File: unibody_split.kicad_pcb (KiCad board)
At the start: 2 copper layers, 305.5 x 82.5 mm, 92 parts, among them J1 Conn_01x02, U1 nice_nano

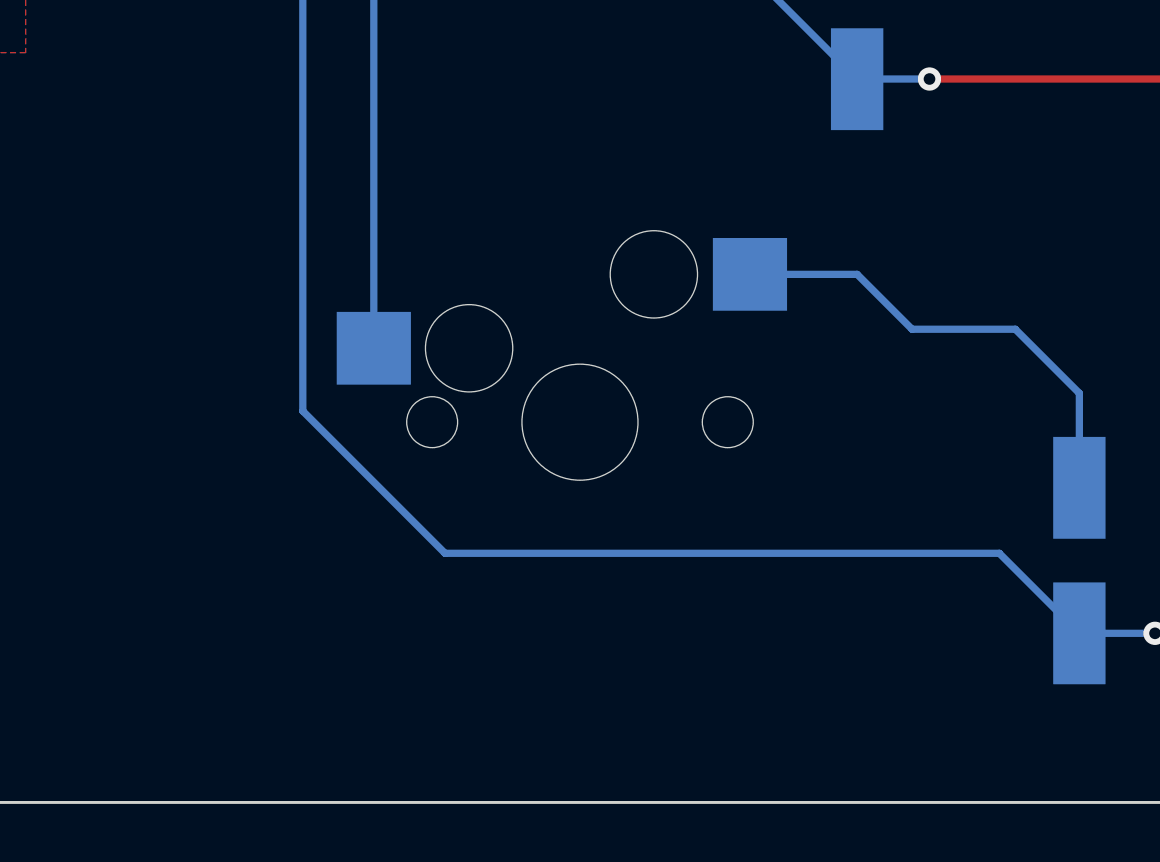
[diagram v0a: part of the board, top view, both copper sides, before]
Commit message: Fixes M29 using wrong footprint
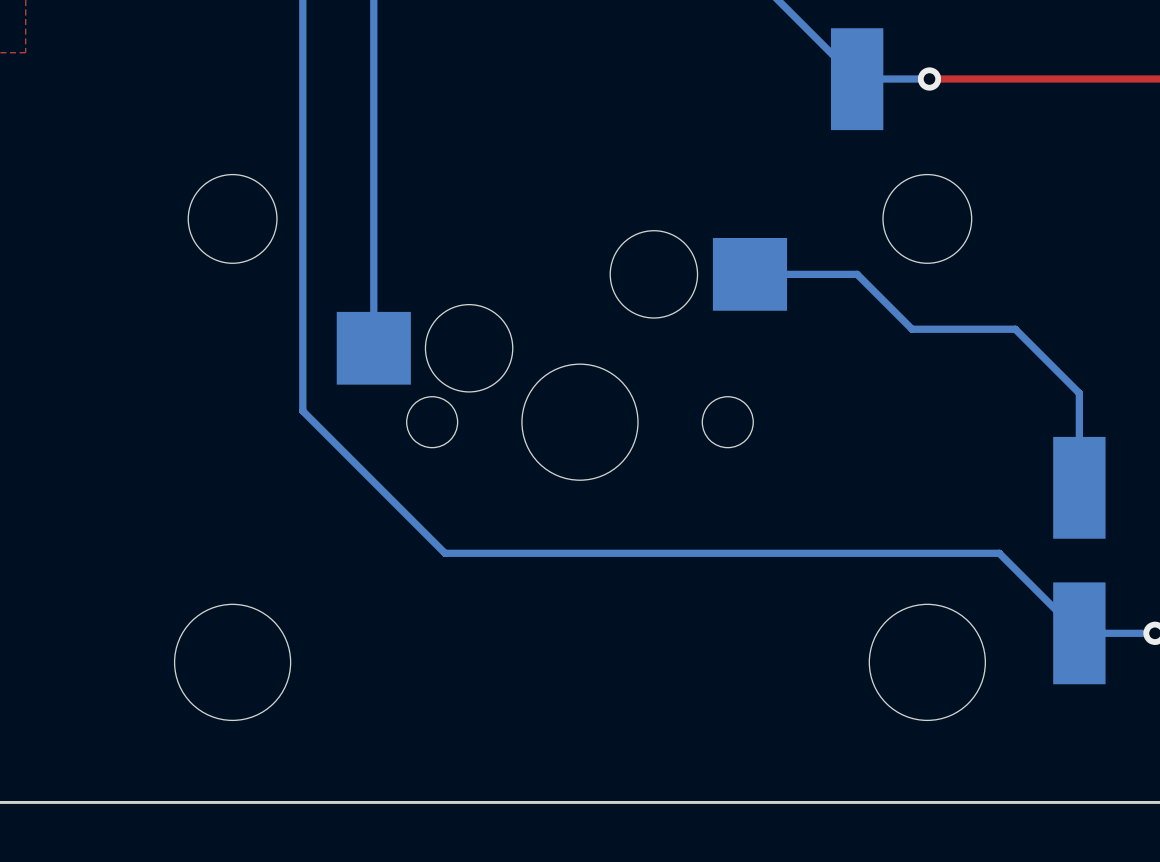
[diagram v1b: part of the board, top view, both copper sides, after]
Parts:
- MX29: footprint MX_Only:MXOnly-1U-Hotswap -> MX_Only:MXOnly-2U-Hotswap
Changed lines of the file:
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@@
     )
   )
-  (footprint "MX_Only:MXOnly-1U-Hotswap" (layer "F.Cu")
+  (footprint "MX_Only:MXOnly-2U-Hotswap" (layer "F.Cu")
     (at 255.5875 165.89375)
     (property "Sheetfile" "unibody_split.kicad_sch")
@@
       (effects (font (size 1 1) (thickness 0.15)))
     )
+    (fp_line (start 19.05 -9.525) (end 19.05 9.525) (layer "Dwgs.User") (width 0.15))
+    (fp_line (start -7 7) (end -5 7) (layer "Dwgs.User") (width 0.15))
+    (fp_line (start 19.05 9.525) (end -19.05 9.525) (layer "Dwgs.User") (width 0.15))
     (fp_line (start -7 -7) (end -7 -5) (layer "Dwgs.User") (width 0.15))
-    (fp_line (start -7 7) (end -5 7) (layer "Dwgs.User") (width 0.15))
+    (fp_line (start 5 -7) (end 7 -7) (layer "Dwgs.User") (width 0.15))
+    (fp_line (start 5 7) (end 7 7) (layer "Dwgs.User") (width 0.15))
+    (fp_line (start 7 7) (end 7 5) (layer "Dwgs.User") (width 0.15))
+    (fp_line (start -7 5) (end -7 7) (layer "Dwgs.User") (width 0.15))
+    (fp_line (start -19.05 9.525) (end -19.05 -9.525) (layer "Dwgs.User") (width 0.15))
+    (fp_line (start -5 -7) (end -7 -7) (layer "Dwgs.User") (width 0.15))
     (fp_line (start 7 -7) (end 7 -5) (layer "Dwgs.User") (width 0.15))
-    (fp_line (start -5 -7) (end -7 -7) (layer "Dwgs.User") (width 0.15))
-    (fp_line (start 7 7) (end 7 5) (layer "Dwgs.User") (width 0.15))
-    (fp_line (start -9.525 -9.525) (end 9.525 -9.525) (layer "Dwgs.User") (width 0.15))
-    (fp_line (start 9.525 -9.525) (end 9.525 9.525) (layer "Dwgs.User") (width 0.15))
-    (fp_line (start -9.525 9.525) (end -9.525 -9.525) (layer "Dwgs.User") (width 0.15))
-    (fp_line (start -7 5) (end -7 7) (layer "Dwgs.User") (width 0.15))
-    (fp_line (start 9.525 9.525) (end -9.525 9.525) (layer "Dwgs.User") (width 0.15))
-    (fp_line (start 5 7) (end 7 7) (layer "Dwgs.User") (width 0.15))
-    (fp_line (start 5 -7) (end 7 -7) (layer "Dwgs.User") (width 0.15))
+    (fp_line (start -19.05 -9.525) (end 19.05 -9.525) (layer "Dwgs.User") (width 0.15))
+    (fp_line (start 7.112 -3.81) (end 4.572 -3.81) (layer "B.CrtYd") (width 0.15))
+    (fp_line (start 5.3 -7) (end 5.3 -2.6) (layer "B.CrtYd") (width 0.127))
+    (fp_line (start -8.382 -3.81) (end -5.842 -3.81) (layer "B.CrtYd") (width 0.15))
+    (fp_line (start -6.5 -4.5) (end -6.5 -0.6) (layer "B.CrtYd") (width 0.127))
+    (fp_line (start -8.382 -1.27) (end -8.382 -3.81) (layer "B.CrtYd") (width 0.15))
     (fp_line (start -6.5 -0.6) (end -2.4 -0.6) (layer "B.CrtYd") (width 0.127))
-    (fp_line (start -5.842 -1.27) (end -5.842 -3.81) (layer "B.CrtYd") (width 0.15))
-    (fp_line (start 5.3 -7) (end 5.3 -2.6) (layer "B.CrtYd") (width 0.127))
-    (fp_line (start 7.112 -3.81) (end 4.572 -3.81) (layer "B.CrtYd") (width 0.15))
-    (fp_line (start -8.382 -3.81) (end -8.382 -1.27) (layer "B.CrtYd") (width 0.15))
+    (fp_line (start -5.842 -3.81) (end -5.842 -1.27) (layer "B.CrtYd") (width 0.15))
+    (fp_line (start 4.572 -6.35) (end 7.112 -6.35) (layer "B.CrtYd") (width 0.15))
+    (fp_line (start -5.842 -1.27) (end -8.382 -1.27) (layer "B.CrtYd") (width 0.15))
+    (fp_line (start 5.3 -7) (end -4 -7) (layer "B.CrtYd") (width 0.127))
     (fp_line (start 4.572 -3.81) (end 4.572 -6.35) (layer "B.CrtYd") (width 0.15))
-    (fp_line (start -8.382 -1.27) (end -5.842 -1.27) (layer "B.CrtYd") (width 0.15))
-    (fp_line (start -6.5 -4.5) (end -6.5 -0.6) (layer "B.CrtYd") (width 0.127))
-    (fp_line (start 4.572 -6.35) (end 7.112 -6.35) (layer "B.CrtYd") (width 0.15))
-    (fp_line (start -5.842 -3.81) (end -8.382 -3.81) (layer "B.CrtYd") (width 0.15))
+    (fp_line (start 7.112 -6.35) (end 7.112 -3.81) (layer "B.CrtYd") (width 0.15))
     (fp_line (start -0.4 -2.6) (end 5.3 -2.6) (layer "B.CrtYd") (width 0.127))
-    (fp_line (start 5.3 -7) (end -4 -7) (layer "B.CrtYd") (width 0.127))
-    (fp_line (start 7.112 -6.35) (end 7.112 -3.81) (layer "B.CrtYd") (width 0.15))
     (fp_arc (start -6.5 -4.5) (mid -5.767767 -6.267767) (end -4 -7) (layer "B.CrtYd") (width 0.127))
     (fp_arc (start -2.4 -0.6) (mid -1.814214 -2.014214) (end -0.4 -2.6) (layer "B.CrtYd") (width 0.127))
     (fp_circle (center -3.81 -2.54) (end -3.81 -4.064) (layer "B.CrtYd") (width 0.15) (fill none))
     (fp_circle (center 2.54 -5.08) (end 2.54 -6.604) (layer "B.CrtYd") (width 0.15) (fill none))
+    (pad "" np_thru_hole circle (at 2.54 -5.08) (size 3 3) (drill 3) (layers *.Cu *.Mask))
+    (pad "" np_thru_hole circle (at 11.938 -6.985) (size 3.048 3.048) (drill 3.048) (layers *.Cu *.Mask))
+    (pad "" np_thru_hole circle (at -11.938 8.255) (size 3.9878 3.9878) (drill 3.9878) (layers *.Cu *.Mask))
+    (pad "" np_thru_hole circle (at 5.08 0 48.0996) (size 1.75 1.75) (drill 1.75) (layers *.Cu *.Mask))
+    (pad "" np_thru_hole circle (at 11.938 8.255) (size 3.9878 3.9878) (drill 3.9878) (layers *.Cu *.Mask))
+    (pad "" np_thru_hole circle (at -3.81 -2.54) (size 3 3) (drill 3) (layers *.Cu *.Mask))
+    (pad "" np_thru_hole circle (at -11.938 -6.985) (size 3.048 3.048) (drill 3.048) (layers *.Cu *.Mask))
     (pad "" np_thru_hole circle (at 0 0) (size 3.9878 3.9878) (drill 3.9878) (layers *.Cu *.Mask))
-    (pad "" np_thru_hole circle (at 5.08 0 48.0996) (size 1.75 1.75) (drill 1.75) (layers *.Cu *.Mask))
     (pad "" np_thru_hole circle (at -5.08 0 48.0996) (size 1.75 1.75) (drill 1.75) (layers *.Cu *.Mask))
-    (pad "" np_thru_hole circle (at 2.54 -5.08) (size 3 3) (drill 3) (layers *.Cu *.Mask))
-    (pad "" np_thru_hole circle (at -3.81 -2.54) (size 3 3) (drill 3) (layers *.Cu *.Mask))
     (pad "1" smd rect (at -7.085 -2.54) (size 2.55 2.5) (layers "B.Cu" "B.Paste" "B.Mask")
       (net 55 "COL6") (pinfunction "COL") (pintype "passive"))
@@
     (model "${KIPRJMOD}/MX_Alps_Hybrid.pretty/MX_Only.pretty/3d_shapes/CPG151101S11.wrl"
       (offset (xyz 0 0 -1.4868))
-      (scale (xyz 0.393701 0.3937 0.393701))
+      (scale (xyz 0.3937 0.3937 0.3937))
       (rotate (xyz 0 0 0))
     )
-    (model "/home/nick/3D Printing/STLs/MX Series-Cherry Key.STEP"
+    (model "${KIPRJMOD}/MX Series-Cherry Key.STEP"
       (offset (xyz 7.35 7.35 6))
       (scale (xyz 1 1 1))
       (rotate (xyz -90 0 180))
     )
+    (model "${KIPRJMOD}/Stabilizer - close.STEP"
+      (offset (xyz -12 0 3.75))
+      (scale (xyz 1 1 1))
+      (rotate (xyz -90 0 0))
+    )
   )

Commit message: Adds mounting holes
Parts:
- added REF**: MountingHole_3.2mm_M3, MountingHole:MountingHole_3.2mm_M3, F.Cu at (328.5, 161.5)
- added REF**: MountingHole_3.2mm_M3, MountingHole:MountingHole_3.2mm_M3, F.Cu at (334.0, 120.0)
- added REF**: MountingHole_3.2mm_M3, MountingHole:MountingHole_3.2mm_M3, F.Cu at (179.5, 105.0)
- added REF**: MountingHole_3.2mm_M3, MountingHole:MountingHole_3.2mm_M3, F.Cu at (185.0, 170.0)
- added REF**: MountingHole_3.2mm_M3, MountingHole:MountingHole_3.2mm_M3, F.Cu at (231.0, 170.0)
- added REF**: MountingHole_3.2mm_M3, MountingHole:MountingHole_3.2mm_M3, F.Cu at (82.8, 119.8)
- added REF**: MountingHole_3.2mm_M3, MountingHole:MountingHole_3.2mm_M3, F.Cu at (227.5, 101.5)
- added REF**: MountingHole_3.2mm_M3, MountingHole:MountingHole_3.2mm_M3, F.Cu at (87.5, 170.0)
- moved D1 1.07 mm to (79.0, 112.5)
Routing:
- net Net-(D1-Pad2): track 9.91 -> 8.75 mm
- net ROW0: track 284.5 -> 285.3 mm
